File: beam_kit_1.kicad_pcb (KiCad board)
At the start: 2 copper layers, 143 parts, among them J1 PZ2.54-2*20, J10 SONAR, J11 NRF, J12 BTN_KNOB, J13 BTN_KNOB, J14 KNOB_AND_WS, J2 PZ2.54-2*20, J3 USB_C_Receptacle, J4 probe_debug, J5 Micro_SD_Card, J6 micro_sd, J7 SSD1306_128x32_OLED, J8 HC-SR04, J9 NRF_24_socket, SW1 BOOTSEL, SW2 BOOTSEL, SW3 RUN, SW4 BTN1, SW5 BTN0, SW6 BTN2, U1 LIS3DH, U2 APDS-9306-065, U3 SN74LVC1G14DBV, U4 M24256-BR (MB85RC16V), U5 RP2040, U6 SN74LVC1G14DBV, U7 W25Q16JVSS, U8 MT3608, U9 SHT30-DIS, Y1 12 MHz

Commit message: fit test
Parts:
- removed SW3: RUN, Button_Switch_SMD:SW_Push_1P1T_NO_6x6mm_H9.5mm
- added C53: 100n 50V, Capacitor_SMD:C_0603_1608Metric, F.Cu at (146.0, 142.8)
- added C54: 10u 10V, Capacitor_SMD:C_0603_1608Metric, F.Cu at (146.0, 145.4)
- added C55: 100n 50V, Capacitor_SMD:C_0603_1608Metric, F.Cu at (146.0, 147.9)
- added C56: 10u 10V, Capacitor_SMD:C_0603_1608Metric, F.Cu at (146.0, 150.4)
- added C57: 100n 50V, Capacitor_SMD:C_0603_1608Metric, F.Cu at (146.0, 152.9)
- added J15: dbg, Connector_JST:JST_SH_BM03B-SRSS-TB_1x03-1MP_P1.00mm_Vertical, F.Cu at (106.5, 94.5)
- added J16: dbg, Connector_JST:JST_SH_BM03B-SRSS-TB_1x03-1MP_P1.00mm_Vertical, F.Cu at (106.5, 108.4)
- added J17: dbg, Connector_JST:JST_SH_BM03B-SRSS-TB_1x03-1MP_P1.00mm_Vertical, F.Cu at (112.9, 94.5)
- added J18: dbg, Connector_JST:JST_SH_BM03B-SRSS-TB_1x03-1MP_P1.00mm_Vertical, F.Cu at (113.0, 108.4)
- added J19: SONAR, Connector_PinHeader_2.54mm:PinHeader_1x03_P2.54mm_Vertical, F.Cu at (146.6, 156.8)
- added J20: micro_sd, Connector_PinHeader_2.54mm:PinHeader_1x06_P2.54mm_Vertical, F.Cu at (137.3, 143.9)
- added J21: NRF_24_socket, Connector_PinSocket_2.54mm:PinSocket_2x04_P2.54mm_Vertical, F.Cu at (153.0, 143.9)
- added J22: SSD1306_128x32_OLED, Connector_PinSocket_2.54mm:PinSocket_1x04_P2.54mm_Vertical, F.Cu at (154.8, 131.5)
- added JP5: NO, Jumper:SolderJumper-2_P1.3mm_Open_RoundedPad1.0x1.5mm, F.Cu at (151.1, 160.3)
- added R21: 2k2 1%, Resistor_SMD:R_0603_1608Metric_Pad0.98x0.95mm_HandSolder, F.Cu at (141.8, 142.8)
- added R22: 2k2 1%, Resistor_SMD:R_0603_1608Metric_Pad0.98x0.95mm_HandSolder, F.Cu at (141.8, 145.4)
- added R23: 10k 1%, Resistor_SMD:R_0603_1608Metric_Pad0.98x0.95mm_HandSolder, F.Cu at (141.8, 147.9)
- added R24: 10k 1%, Resistor_SMD:R_0603_1608Metric_Pad0.98x0.95mm_HandSolder, F.Cu at (141.8, 150.4)
- added R25: 2k2 1%, Resistor_SMD:R_0603_1608Metric_Pad0.98x0.95mm_HandSolder, F.Cu at (141.8, 152.9)
- added R26: 2k2 1%, Resistor_SMD:R_0603_1608Metric_Pad0.98x0.95mm_HandSolder, F.Cu at (141.8, 155.4)
- added R27: 100R 1%, Resistor_SMD:R_0603_1608Metric_Pad0.98x0.95mm_HandSolder, F.Cu at (102.6, 111.8)
- added R28: 100R 1%, Resistor_SMD:R_0603_1608Metric_Pad0.98x0.95mm_HandSolder, F.Cu at (102.6, 105.0)
- added R29: 100R 1%, Resistor_SMD:R_0603_1608Metric_Pad0.98x0.95mm_HandSolder, F.Cu at (87.2, 100.4)
- added R30: 100R 1%, Resistor_SMD:R_0603_1608Metric_Pad0.98x0.95mm_HandSolder, F.Cu at (87.2, 101.9)
- added SW7: RUN, Button_Switch_SMD:SW_SPST_B3U-1000P, F.Cu at (186.0, 93.0)
- added U10: SHT30-DIS, Sensor_Humidity:Sensirion_DFN-8-1EP_2.5x2.5mm_P0.5mm_EP1.1x1.7mm, F.Cu at (151.5, 156.5)
- J10: value SONAR -> UART_SEPARATOR; footprint Connector_PinHeader_2.54mm:PinHeader_1x03_P2.54mm_Vertical -> Connector_PinHeader_2.54mm:PinHeader_2x02_P2.54mm_Vertical
- J6: value micro_sd -> OLED I2C; footprint Connector_PinHeader_2.54mm:PinHeader_1x06_P2.54mm_Vertical -> Connector_PinHeader_2.54mm:PinHeader_1x02_P2.54mm_Vertical
- J7: value SSD1306_128x32_OLED -> VL53_PINS; footprint Connector_PinSocket_2.54mm:PinSocket_1x04_P2.54mm_Vertical -> Connector_PinHeader_2.54mm:PinHeader_1x02_P2.54mm_Vertical
- J9: value NRF_24_socket -> I2C; footprint Connector_PinSocket_2.54mm:PinSocket_2x04_P2.54mm_Vertical -> Connector_PinHeader_2.54mm:PinHeader_1x02_P2.54mm_Vertical
- SW1: footprint Button_Switch_SMD:SW_Push_1P1T_NO_6x6mm_H9.5mm -> Button_Switch_SMD:SW_SPST_B3U-1000P
- SW2: value BOOTSEL -> RUN; footprint Button_Switch_SMD:SW_Push_1P1T_NO_6x6mm_H9.5mm -> Button_Switch_SMD:SW_SPST_B3U-1000P
- U4: value M24256-BR (MB85RC16V) -> M24256-BR
- U9: value SHT30-DIS -> VL53L0CXV0DH1; footprint Sensor_Humidity:Sensirion_DFN-8-1EP_2.5x2.5mm_P0.5mm_EP1.1x1.7mm -> Sensor_Distance:ST_VL53L1x
- moved C36 159.8 mm to (84.0, 162.1), turned to 90 degrees
- moved C48 156.7 mm to (90.7, 162.1), turned to 90 degrees
- moved C37 153.9 mm to (84.0, 154.0), turned to 90 degrees
- moved C39 153.1 mm to (90.7, 154.0), turned to 90 degrees
- moved C40 151.6 mm to (97.2, 162.1), turned to 90 degrees
- moved C45 150.9 mm to (90.7, 145.9), turned to 90 degrees
- moved C49 149.2 mm to (90.7, 137.8), turned to 90 degrees
- moved C38 148.6 mm to (84.0, 145.9), turned to 90 degrees
- moved C44 147.1 mm to (84.0, 137.7), turned to 90 degrees
- moved U4 146.4 mm to (88.0, 121.0), turned to 90 degrees
- moved C43 145.5 mm to (97.2, 154.0), turned to 90 degrees
- moved U2 145.1 mm to (93.0, 119.7), turned to 90 degrees
- moved C52 143.6 mm to (103.9, 154.0), turned to 90 degrees
- moved C47 143.2 mm to (97.2, 145.9), turned to 90 degrees
- moved RV2 142.4 mm to (116.6, 160.8)
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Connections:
- J10 pad 1: /peripheral/SONAR_TRIG -> /prog/TARGET_RX
- J10 pad 2: /peripheral/SONAR_ECHO -> /GPIO1
- J10 pad 3: /peripheral/SON_EN -> /prog/TARGET_TX
- J5 pad 1: /peripheral/SD_DAT2 -> Net-(J20-Pin_1)
- J5 pad 2: /peripheral/GPIO22 -> Net-(J20-Pin_2)
- J5 pad 3: /peripheral/GPIO18 -> Net-(J20-Pin_3)
- J5 pad 5: /peripheral/GPIO5 -> Net-(J20-Pin_4)
- J5 pad 7: /peripheral/GPIO19 -> Net-(J20-Pin_5)
- J5 pad 8: /peripheral/SD_DAT1 -> Net-(J20-Pin_6)
- J6 pad 1: /peripheral/SD_DAT2 -> /peripheral/OLED_SDA
- J6 pad 2: /peripheral/GPIO22 -> /peripheral/OLED_SCL
- J7 pad 1: /peripheral/OLED_SDA -> Net-(J7-Pin_1)
- J7 pad 2: /peripheral/OLED_SCL -> Net-(J7-Pin_2)
- J9 pad 1: GND -> /peripheral/SCL
- J9 pad 2: +3V3 -> /peripheral/SDA
- JP1 pad 2: /prog/TARGET_TX -> Net-(JP1-B)
- JP2 pad 2: /prog/TARGET_RX -> Net-(JP2-B)
- JP3 pad 2: /prog/TARGET_RX -> Net-(JP2-B)
- JP4 pad 2: /prog/TARGET_TX -> Net-(JP1-B)
- R11 pad 1: /peripheral/SD_DAT2 -> Net-(J20-Pin_1)
- R13 pad 1: /peripheral/GPIO5 -> Net-(J20-Pin_4)
- R9 pad 1: /peripheral/SD_DAT1 -> Net-(J20-Pin_6)
- U1 pad 1: unconnected-(U1-VDD_IO-Pad1) -> +3V3
- U1 pad 10: Net-(U1-GND-Pad10) -> GND
- U1 pad 12: Net-(U1-GND-Pad10) -> GND
- U1 pad 13: unconnected-(U1-ADC3-Pad13) -> GND
- U1 pad 14: unconnected-(U1-VDD-Pad14) -> +3V3
- U1 pad 15: unconnected-(U1-ADC2-Pad15) -> GND
- U1 pad 16: unconnected-(U1-ADC1-Pad16) -> GND
- U1 pad 4: unconnected-(U1-SPC-Pad4) -> /peripheral/SCL
- U1 pad 5: Net-(U1-GND-Pad10) -> GND
- U1 pad 6: unconnected-(U1-SDI-Pad6) -> /peripheral/SDA
- U1 pad 7: unconnected-(U1-SDO-Pad7) -> Net-(JP5-B)
- U1 pad 8: unconnected-(U1-CS-Pad8) -> +3V3
- U5 pad 4: /prog/TARGET_SWCLK -> Net-(U5-GPIO2)
- U5 pad 5: /prog/TARGET_SWDIO -> Net-(U5-GPIO3)
- U9 pad 1: (no net) -> +3V3
- U9 pad 2: (no net) -> GND
- U9 pad 3: (no net) -> GND
- U9 pad 4: (no net) -> GND
- U9 pad 5: (no net) -> Net-(J7-Pin_2)
- U9 pad 6: (no net) -> GND
- U9 pad 7: (no net) -> Net-(J7-Pin_1)
- U9 pad 8: (no net) -> unconnected-(U9-DNC-Pad8)
- U9 pad 9: (no net) -> /peripheral/SDA
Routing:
- net +3.3V: track 13.2 -> 37.9 mm
- net Net-(D1-TVS3): track 0.00 -> 17.5 mm, vias 0 -> 4
- net Net-(U5-VREG_VOUT): track 0.00 -> 15.2 mm
- net Net-(D1-TVS1): track 0.00 -> 14.8 mm, vias 0 -> 3
- net Net-(D2-A): track 0.00 -> 12.7 mm
- net /prog/QSPI_D3: track 0.00 -> 6.73 mm, vias 0 -> 2
- net GND: track 127.7 -> 132.7 mm
- net /prog/QSPI_SCK: track 0.00 -> 4.89 mm, vias 0 -> 2
- net Net-(D3-A): track 0.00 -> 4.03 mm
- net /prog/QSPI_CS: track 0.00 -> 3.76 mm
- net /prog/QSPI_D0: track 0.00 -> 3.53 mm, vias 0 -> 2
- net /prog/USB_DM: track 0.00 -> 3.27 mm
- net Net-(U5-GPIO3): track 0.00 -> 3.23 mm
- net /prog/QSPI_D2: track 0.00 -> 2.80 mm, vias 0 -> 2
- net Net-(U5-GPIO2): track 0.00 -> 2.77 mm
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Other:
- board outline added: 110 x 90 mm
- board text added: "B0"
- board text added: "B1"
- board text added: "B2"
- board text added: "BTN 0"
- board text added: "BTN 1"
- board text added: "BTN 2"
- board text added: "L0"
- board text added: "L1"
- board text added: "L2"
- board text added: "LED 0"
- board text added: "LED 1"
- board text added: "LED 2"

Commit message: layout
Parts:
- added H1: Hole, MountingHole:MountingHole_3.2mm_M3_Pad_Via, F.Cu at (209.0, 57.0)
- added H2: Hole, MountingHole:MountingHole_3.2mm_M3_Pad_Via, F.Cu at (209.0, 143.0)
- added H3: Hole, MountingHole:MountingHole_3.2mm_M3_Pad_Via, F.Cu at (94.0, 57.0)
- added H4: Hole, MountingHole:MountingHole_3.2mm_M3_Pad_Via, F.Cu at (151.0, 112.0)
- added H5: Hole, MountingHole:MountingHole_3.2mm_M3_Pad_Via, F.Cu at (94.0, 143.0)
- added H6: MB template, MountingHole:MountingHole_2.1mm, F.Cu at (114.8, 52.6)
- added H6: MB template, MountingHole:MountingHole_2.1mm, F.Cu at (114.8, 83.3)
- added H6: MB template, MountingHole:MountingHole_2.1mm, F.Cu at (114.8, 71.8)
- added H6: MB template, MountingHole:MountingHole_2.1mm, F.Cu at (114.8, 69.5)
- added H6: MB template, MountingHole:MountingHole_2.1mm, F.Cu at (89.8, 96.3)
- added H6: MB template, MountingHole:MountingHole_2.1mm, F.Cu at (114.8, 74.0)
- added H6: MB template, MountingHole:MountingHole_2.1mm, F.Cu at (114.8, 70.7)
- added H6: MB template, MountingHole:MountingHole_2.1mm, F.Cu at (114.8, 72.8)
- added H6: MB template, MountingHole:MountingHole_2.1mm, F.Cu at (114.8, 84.4)
- added H6: MB template, MountingHole:MountingHole_2.1mm, F.Cu at (114.8, 87.7)
- added H6: MB template, MountingHole:MountingHole_2.1mm, F.Cu at (114.8, 86.6)
- added H6: MB template, MountingHole:MountingHole_2.1mm, F.Cu at (114.8, 85.5)
- moved J8 99.5 mm to (212.0, 84.6), turned to 180 degrees
- moved U6 97.4 mm to (207.7, 83.6), turned to 90 degrees
- moved J14 93.7 mm to (94.5, 122.1), turned to 180 degrees
- moved C42 91.4 mm to (91.1, 126.9)
- moved C53 89.9 mm to (58.0, 161.4)
- moved C54 89.9 mm to (58.0, 163.9)
- moved C55 89.9 mm to (58.0, 166.4)
- moved C56 89.9 mm to (58.0, 168.9)
- moved C57 89.9 mm to (58.0, 171.4)
- moved J21 89.9 mm to (65.0, 162.5)
- moved JP5 89.9 mm to (63.1, 178.8)
- moved L1 89.9 mm to (44.7, 164.5)
- moved R21 89.9 mm to (53.8, 161.4)
- moved R22 89.9 mm to (53.8, 163.9)
- moved R23 89.9 mm to (53.8, 166.4)
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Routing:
- net /prog/QSPI_D3: track 6.73 -> 1.62 mm, vias 2 -> 1
- net Net-(D3-A): track 4.03 -> 0.00 mm
- net /prog/QSPI_SCK: track 4.89 -> 1.77 mm, vias 2 -> 1
- net /prog/QSPI_D0: track 3.53 -> 1.77 mm, vias 2 -> 1
- net /prog/QSPI_D2: track 2.80 -> 1.29 mm, vias 2 -> 1
- net Net-(U5-GPIO25): track 2.57 -> 1.13 mm, vias 2 -> 1
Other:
- board size 110 x 90 mm -> 125 x 96 mm
- board text added: "CLK"
- board text added: "CMD"
- board text added: "DAT0"
- board text added: "DAT1"
- board text added: "DAT2"
- board text added: "DAT3"
- board text added: "ECHO"
- board text added: "ENA"
- board text added: "POT"
- board text added: "TRIG"
- board text added: "USER BUTTONS"
- board text added: "USER LEDs"
- board text added: "WS"
- board text added: "microSD"
- board text removed: "SONAR DIR"

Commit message: layout
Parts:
- added H7: Hole, MountingHole:MountingHole_3.2mm_M3_Pad_Via, F.Cu at (132.8, 108.5)
- L1: footprint Inductor_SMD:L_Wuerth_MAPI-3020 -> Inductor_SMD:L_1206_3216Metric_Pad1.22x1.90mm_HandSolder
- R17: footprint Resistor_SMD:R_0603_1608Metric -> Resistor_SMD:R_0603_1608Metric_Pad0.98x0.95mm_HandSolder
- moved L1 180.8 mm to (211.6, 94.8), turned to 90 degrees
- moved R17 170.4 mm to (207.3, 72.8)
- moved D14 165.5 mm to (211.6, 89.2), turned to -90 degrees
- moved R18 165.5 mm to (208.2, 90.5), turned to 180 degrees
- moved C32 165.2 mm to (207.2, 78.7)
- moved C35 164.8 mm to (208.2, 87.6), turned to 180 degrees
- moved R19 164.2 mm to (205.7, 90.0), turned to 90 degrees
- moved C34 163.9 mm to (211.2, 98.7), turned to 180 degrees
- moved R16 153.3 mm to (207.3, 74.6), turned to 180 degrees
- moved U8 153.0 mm to (208.1, 94.6), turned to -90 degrees
- moved J21 150.6 mm to (212.1, 130.0)
- moved J10 105.2 mm to (118.0, 54.2)
- moved J11 51.7 mm to (203.7, 129.5)
- moved H4 18.8 mm to (169.5, 108.5)
- moved J12 9.86 mm to (192.3, 131.8)
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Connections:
- J10 pad 1: /prog/TARGET_RX -> /prog/TARGET_TX
- J10 pad 2: /GPIO1 -> /GPIO0
- J10 pad 3: /prog/TARGET_TX -> /prog/TARGET_RX
- J10 pad 4: /GPIO0 -> /GPIO1
- J21 pad 1: GND -> +3V3
- J21 pad 2: +3V3 -> GND
- J21 pad 3: /peripheral/NRF_CE -> /peripheral/NRF_CNS
- J21 pad 4: /peripheral/NRF_CNS -> /peripheral/NRF_CE
- J21 pad 5: /peripheral/NRF_SCK -> /peripheral/NRF_MOSI
- J21 pad 6: /peripheral/NRF_MOSI -> /peripheral/NRF_SCK
- J21 pad 7: /peripheral/NRF_MISO -> /peripheral/NRF_IRQ
- J21 pad 8: /peripheral/NRF_IRQ -> /peripheral/NRF_MISO
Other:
- board text added: "3V3 PICO"
- board text added: "CE"
- board text added: "CNS"
- board text added: "GND"
- board text added: "GPIO0"
- board text added: "GPIO1"
- board text added: "GPIO10"
- board text added: "GPIO11"
- board text added: "GPIO12"
- board text added: "GPIO13"
- board text added: "GPIO14"
- board text added: "GPIO15"
- board text added: "GPIO16"
- board text added: "GPIO17"
- board text added: "GPIO18"
- board text added: "GPIO19"
- board text added: "GPIO2"
- board text added: "GPIO20"
- board text added: "GPIO21"
- board text added: "GPIO22"
- board text added: "GPIO26"
- board text added: "GPIO27"
- board text added: "GPIO28"
- board text added: "GPIO3"
- board text added: "GPIO4"
- board text added: "GPIO5"
- board text added: "GPIO6"
- board text added: "GPIO7"
- board text added: "GPIO8"
- board text added: "GPIO9"
- board text added: "HC-SR04 SONAR SOCKET"
- board text added: "IRQ"
- board text added: "MISO"
- board text added: "MOSI"
- board text added: "NC"
- board text added: "NRF24 SOCKET"
- board text added: "OLED"
- board text added: "RUN"
- board text added: "SCK"
- board text added: "SCL"
- board text added: "SDA"
- board text added: "SONAR"
- board text added: "VBUS"
- board text added: "VSYS"

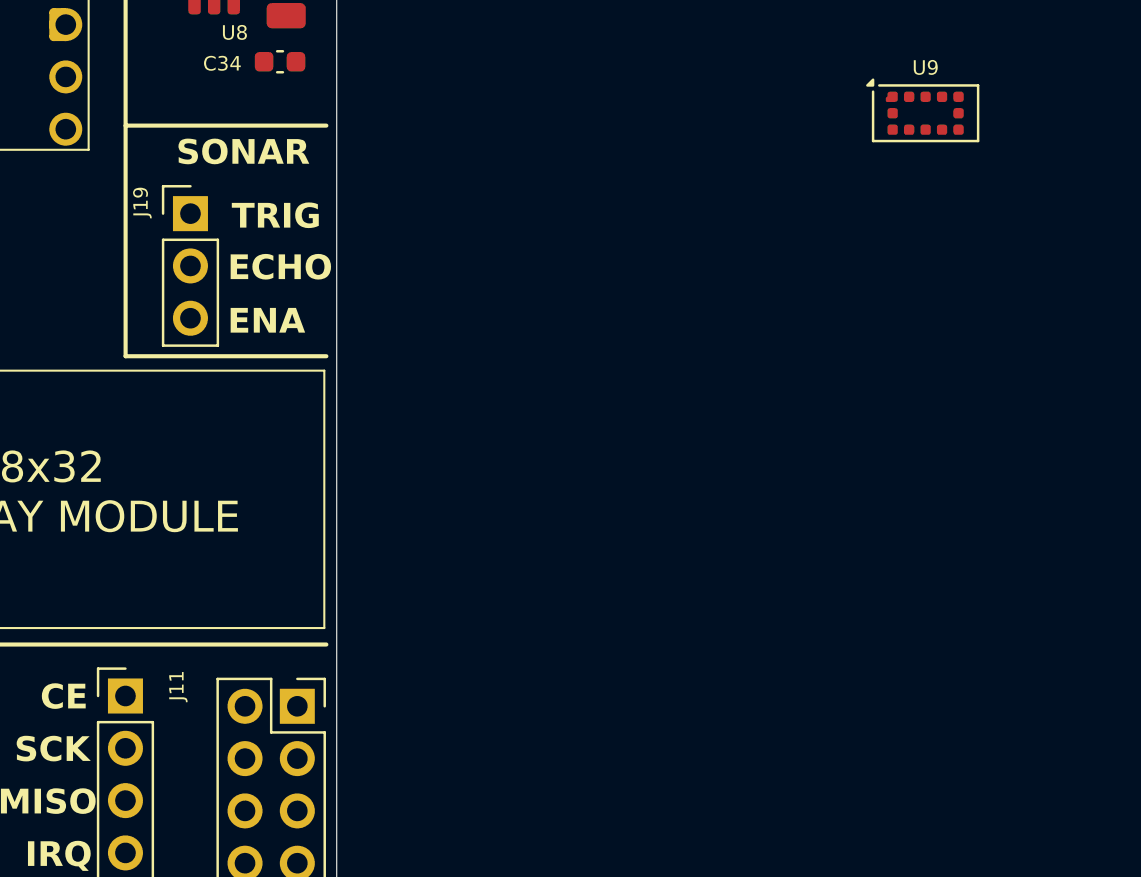
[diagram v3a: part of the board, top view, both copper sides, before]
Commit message: preparing for more modules
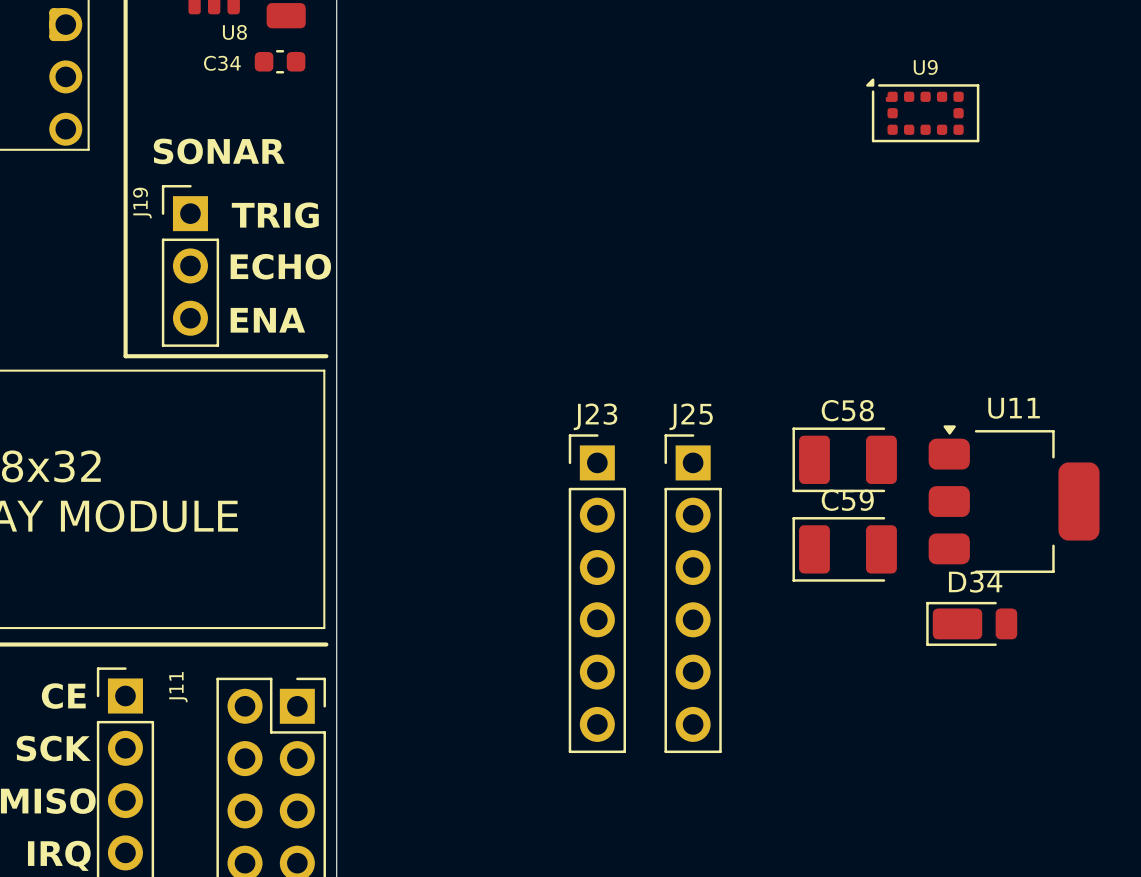
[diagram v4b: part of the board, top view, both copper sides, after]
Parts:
- added C58: 100u 6V3 Tantal, Capacitor_Tantalum_SMD:CP_EIA-3528-21_Kemet-B_Pad1.50x2.35mm_HandSolder, F.Cu at (238.8, 118.0)
- added C59: 100u 6V3 Tantal, Capacitor_Tantalum_SMD:CP_EIA-3528-21_Kemet-B_Pad1.50x2.35mm_HandSolder, F.Cu at (238.8, 122.4)
- added D34: 1A, 30V, Diode_SMD:D_PowerDI-123, F.Cu at (245.0, 126.0)
- added J23: 5V, Connector_PinHeader_2.54mm:PinHeader_1x06_P2.54mm_Vertical, F.Cu at (226.7, 118.2)
- added J25: 3V3, Connector_PinHeader_2.54mm:PinHeader_1x06_P2.54mm_Vertical, F.Cu at (231.3, 118.2)
- added U11: AMS1117-3.3, Package_TO_SOT_SMD:SOT-223-3_TabPin2, F.Cu at (246.9, 120.1)
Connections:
- A1 pad 36: +3.3V -> unconnected-(A1-3V3-Pad36)_1

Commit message: more stuff added to sch
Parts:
- added C60: 100n 50V, Capacitor_SMD:C_0603_1608Metric, F.Cu at (51.8, 48.5)
- added C61: 100n 50V, Capacitor_SMD:C_0603_1608Metric, F.Cu at (51.8, 51.0)
- added C62: 100n 50V, Capacitor_SMD:C_0603_1608Metric, F.Cu at (51.8, 53.5)
- added C63: 47u 6V3, Capacitor_SMD:C_0805_2012Metric, F.Cu at (76.2, 68.9)
- added C64: 100n 50V, Capacitor_SMD:C_0603_1608Metric, F.Cu at (51.8, 56.1)
- added C65: 100n 50V, Capacitor_SMD:C_0603_1608Metric, F.Cu at (51.8, 58.6)
- added C66: 47u 6V3, Capacitor_SMD:C_0805_2012Metric, F.Cu at (76.2, 71.9)
- added C67: 10u 10V, Capacitor_SMD:C_0603_1608Metric, F.Cu at (51.8, 61.1)
- added C68: TBD, Capacitor_SMD:C_0603_1608Metric, F.Cu at (51.8, 63.6)
- added C69: 100n 50V, Capacitor_SMD:C_0603_1608Metric, F.Cu at (51.8, 66.1)
- added C70: 1n 50V, Capacitor_SMD:C_0603_1608Metric, F.Cu at (51.8, 68.6)
- added C71: 100n 50V, Capacitor_SMD:C_0603_1608Metric_Pad1.08x0.95mm_HandSolder, F.Cu at (56.0, 48.5)
- added C72: 100n 50V, Capacitor_SMD:C_0603_1608Metric_Pad1.08x0.95mm_HandSolder, F.Cu at (56.0, 51.0)
- added D35: SMAJ12CA, Diode_SMD:D_SMA, F.Cu at (76.1, 49.5)
- added D36: SMAJ12CA, Diode_SMD:D_SMA, F.Cu at (76.1, 54.1)
- added D37: SMAJ12CA, Diode_SMD:D_SMA, F.Cu at (76.1, 58.6)
- added D38: ESDA6V1BC6, Package_TO_SOT_SMD:SOT-23-6, F.Cu at (69.4, 49.7)
- added D39: ESDA6V1BC6, Package_TO_SOT_SMD:SOT-23-6, F.Cu at (69.4, 54.3)
- added J24: GND, Connector_PinHeader_2.54mm:PinHeader_2x06_P2.54mm_Vertical, F.Cu at (228.7, 138.7)
- added J27: PJ-320D, Connector_Audio:Jack_3.5mm_PJ320D_Horizontal, F.Cu at (63.0, 72.9)
- added J28: screw_term, TerminalBlock_Phoenix:TerminalBlock_Phoenix_MKDS-1,5-2-5.08_1x02_P5.08mm_Horizontal, F.Cu at (41.1, 53.5)
- added J29: screw_term, TerminalBlock_Phoenix:TerminalBlock_Phoenix_MKDS-1,5-2-5.08_1x02_P5.08mm_Horizontal, F.Cu at (41.1, 65.4)
- added J30: RS485, Connector_PinHeader_2.54mm:PinHeader_1x03_P2.54mm_Vertical, F.Cu at (67.2, 80.7)
- added J32: AUDIO, Connector_PinHeader_2.54mm:PinHeader_1x03_P2.54mm_Vertical, F.Cu at (71.8, 80.7)
- added JP6: NC, Jumper:SolderJumper-2_P1.3mm_Bridged_RoundedPad1.0x1.5mm, F.Cu at (71.8, 69.1)
- added JP7: NO, Jumper:SolderJumper-2_P1.3mm_Open_RoundedPad1.0x1.5mm, F.Cu at (71.8, 72.7)
- added MK1: GMI9767P-52DB, Connector_PinHeader_2.54mm:PinHeader_1x02_P2.54mm_Vertical, F.Cu at (76.5, 80.7)
- added R31: 220R 1%, Resistor_SMD:R_0603_1608Metric_Pad0.98x0.95mm_HandSolder, F.Cu at (56.0, 53.5)
- added R32: 100R 1%, Resistor_SMD:R_0603_1608Metric_Pad0.98x0.95mm_HandSolder, F.Cu at (56.0, 56.1)
- added R33: 100R 1%, Resistor_SMD:R_0603_1608Metric_Pad0.98x0.95mm_HandSolder, F.Cu at (56.0, 58.6)
- added R34: 1k8 1%, Resistor_SMD:R_0603_1608Metric_Pad0.98x0.95mm_HandSolder, F.Cu at (56.0, 61.1)
- added R35: 1k8 1%, Resistor_SMD:R_0603_1608Metric_Pad0.98x0.95mm_HandSolder, F.Cu at (56.0, 63.6)
- added R36: 10k 1%, Resistor_SMD:R_0603_1608Metric_Pad0.98x0.95mm_HandSolder, F.Cu at (46.1, 92.7)
- added R37: 220R 1%, Resistor_SMD:R_0603_1608Metric_Pad0.98x0.95mm_HandSolder, F.Cu at (56.0, 66.1)
- added R38: 10k 1%, Resistor_SMD:R_0603_1608Metric_Pad0.98x0.95mm_HandSolder, F.Cu at (39.7, 92.7)
- added R39: 4k7 1%, Resistor_SMD:R_0603_1608Metric_Pad0.98x0.95mm_HandSolder, F.Cu at (60.3, 48.5)
- added R40: 4k7 1%, Resistor_SMD:R_0603_1608Metric_Pad0.98x0.95mm_HandSolder, F.Cu at (60.3, 51.0)
- added R41: 120R 1%, Resistor_SMD:R_0603_1608Metric_Pad0.98x0.95mm_HandSolder, F.Cu at (60.3, 53.5)
- added R42: 120R 1%, Resistor_SMD:R_0603_1608Metric_Pad0.98x0.95mm_HandSolder, F.Cu at (60.3, 56.1)
- added R43: 10k 1%, Resistor_SMD:R_0603_1608Metric_Pad0.98x0.95mm_HandSolder, F.Cu at (60.3, 58.6)
- added R44: 10k 1%, Resistor_SMD:R_0603_1608Metric_Pad0.98x0.95mm_HandSolder, F.Cu at (60.3, 61.1)
- added R45: 10k 1%, Resistor_SMD:R_0603_1608Metric_Pad0.98x0.95mm_HandSolder, F.Cu at (60.3, 63.6)
- added R46: 10k 1%, Resistor_SMD:R_0603_1608Metric_Pad0.98x0.95mm_HandSolder, F.Cu at (60.3, 66.1)
- added R47: 10k 1%, Resistor_SMD:R_0603_1608Metric_Pad0.98x0.95mm_HandSolder, F.Cu at (64.7, 48.5)
- added R48: 2k2 1%, Resistor_SMD:R_0603_1608Metric_Pad0.98x0.95mm_HandSolder, F.Cu at (64.7, 51.0)
- added R49: 10k 1%, Resistor_SMD:R_0603_1608Metric_Pad0.98x0.95mm_HandSolder, F.Cu at (64.7, 53.5)
- added R50: 10k 1%, Resistor_SMD:R_0603_1608Metric_Pad0.98x0.95mm_HandSolder, F.Cu at (64.7, 56.1)
- added R51: 10k 1%, Resistor_SMD:R_0603_1608Metric_Pad0.98x0.95mm_HandSolder, F.Cu at (64.7, 58.6)
- added R52: 10k 1%, Resistor_SMD:R_0603_1608Metric_Pad0.98x0.95mm_HandSolder, F.Cu at (64.7, 61.1)
- added R53: 100R 1%, Resistor_SMD:R_0603_1608Metric_Pad0.98x0.95mm_HandSolder, F.Cu at (64.7, 63.6)
- added RV1: 500k 3386P-1-504TLF, Potentiometer_THT:Potentiometer_Bourns_3386P_Vertical, F.Cu at (59.4, 86.5)
- added U12: SN74LVC1G14DBV, Package_TO_SOT_SMD:SOT-23-5, F.Cu at (69.4, 58.9)
- added U13: SN74LVC1G14DBV, Package_TO_SOT_SMD:SOT-23-5, F.Cu at (69.4, 63.5)
- added U14: MAX485E, Package_SO:SOIC-8_3.9x4.9mm_P1.27mm, F.Cu at (41.8, 74.3)
- added U16: LMV358IDR, Package_SO:SOIC-8_3.9x4.9mm_P1.27mm, F.Cu at (41.8, 80.9)
- J23: value 5V -> 3V3
- J25: value 3V3 -> 5V
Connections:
- J23 pad 1: VBUS -> +3V3
- J23 pad 2: VBUS -> +3V3
- J23 pad 3: VBUS -> +3V3
- J23 pad 4: VBUS -> +3V3
- J23 pad 5: VBUS -> +3V3
- J23 pad 6: VBUS -> +3V3
- J25 pad 1: +3V3 -> VBUS
- J25 pad 2: +3V3 -> VBUS
- J25 pad 3: +3V3 -> VBUS
- J25 pad 4: +3V3 -> VBUS
- J25 pad 5: +3V3 -> VBUS
- J25 pad 6: +3V3 -> VBUS
